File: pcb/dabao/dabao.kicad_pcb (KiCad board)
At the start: 2 copper layers, 127.4 x 114.6 mm, 76 parts, among them J1 Conn_01x05, J2 USB_C_Receptacle_USB2.0_16P, J3 Conn_01x04, J4 MagConn_01x04_Pin, J5 Conn_Battery, J7 Conn_01x04, J8 Display, SW1 SW_RESET, SW2 SW_POWER, U1 nice_nano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

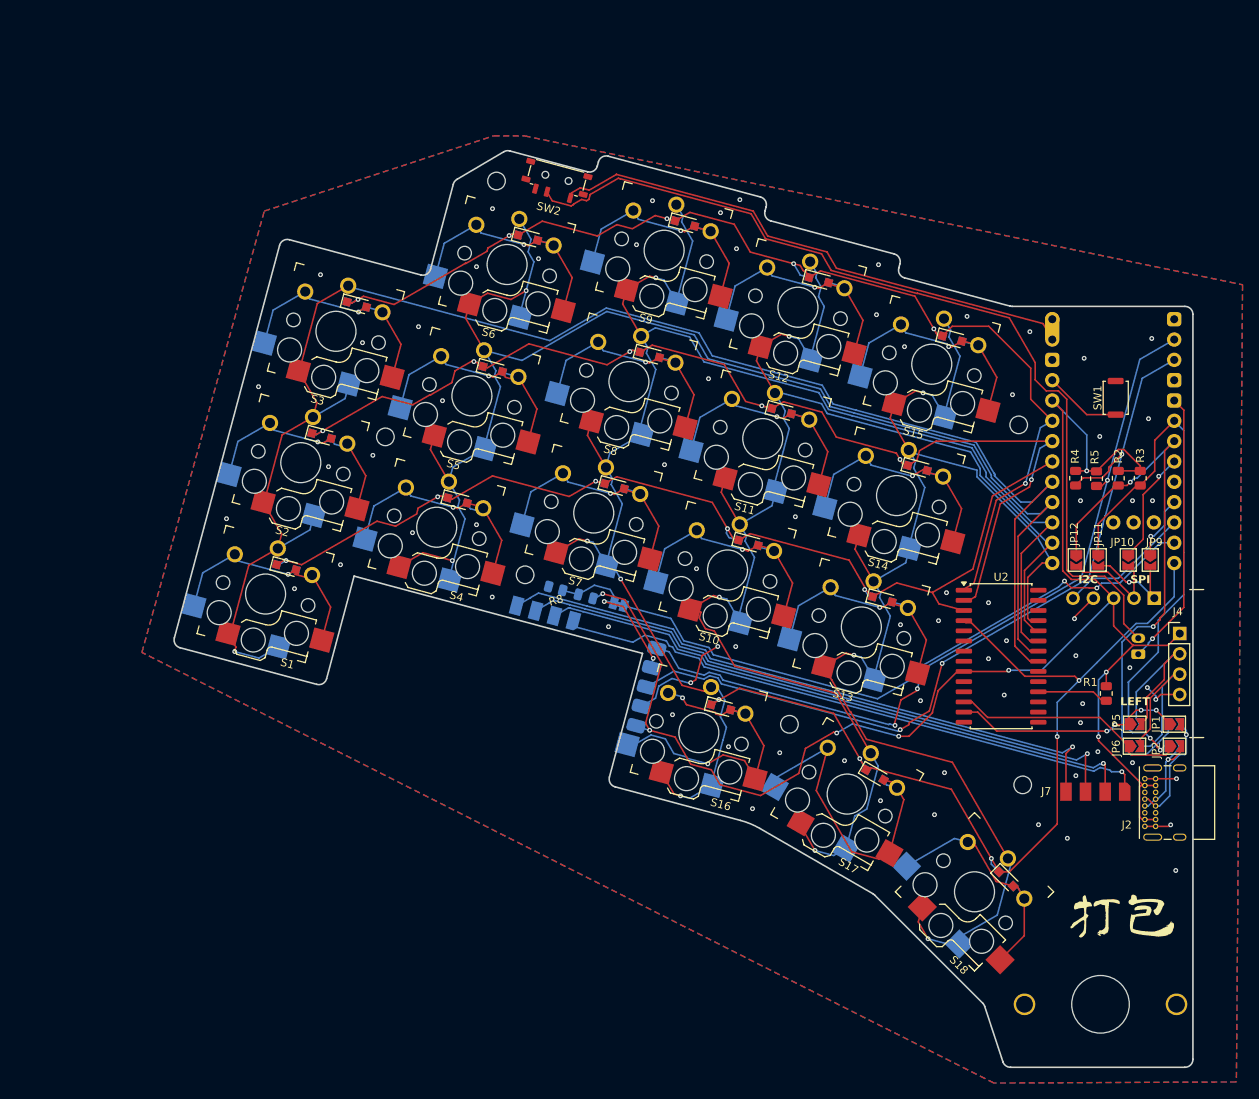
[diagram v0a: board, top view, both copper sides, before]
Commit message: Update outline for mounting holes
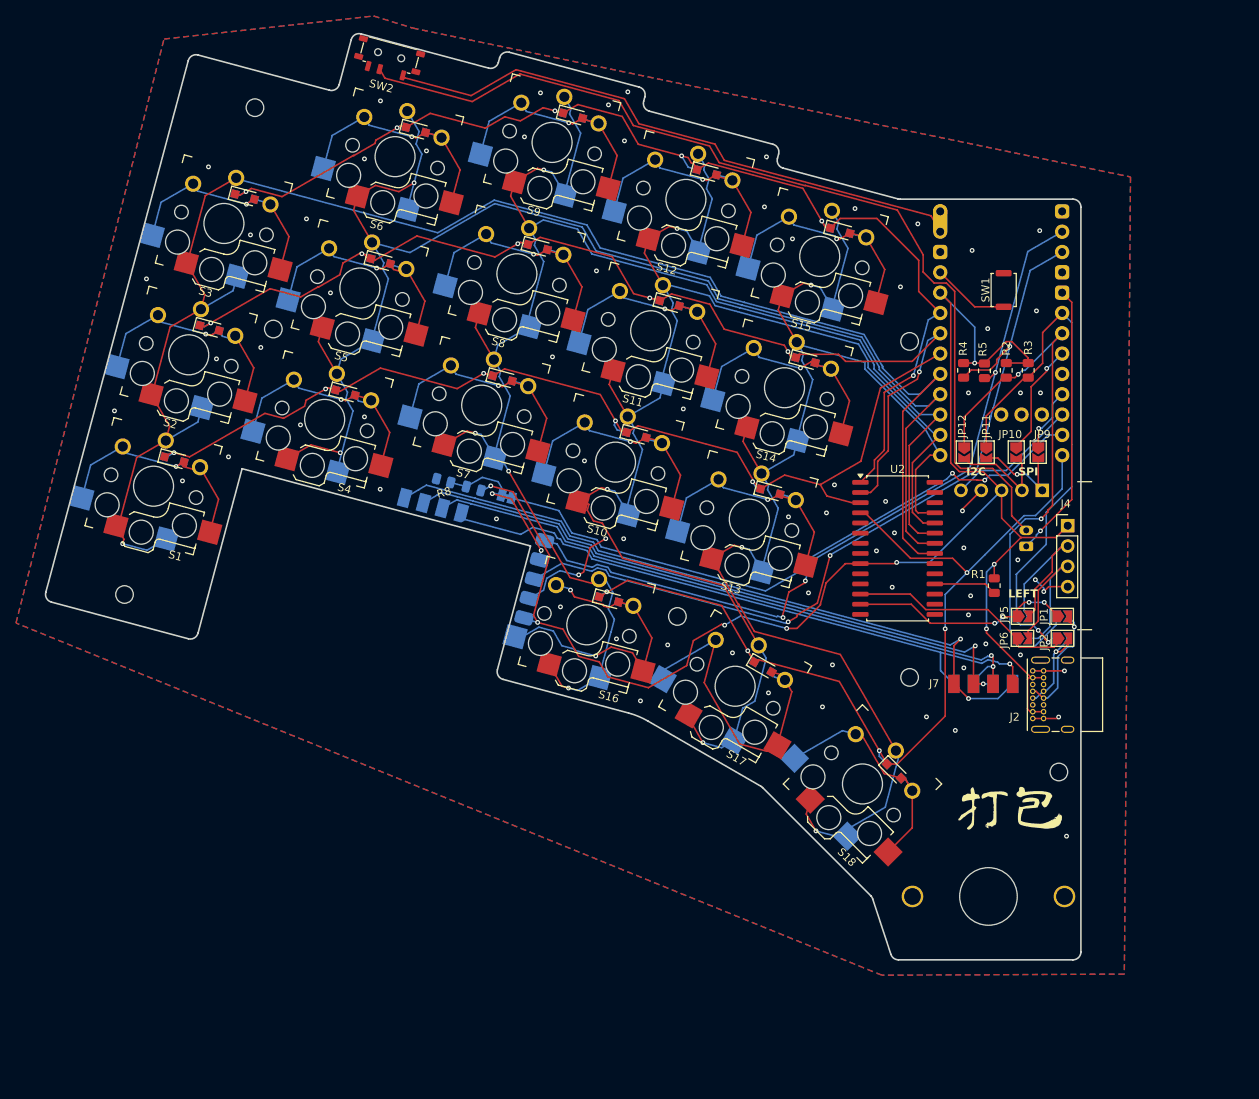
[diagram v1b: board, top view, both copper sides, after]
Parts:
- removed the REF** at (126.4, 98.2)
- added J6: Conn_01x04, Library:TPSensorModule_Connector, B.Cu at (183.7, 111.8)
- added REF**: MountingHole_2.2mm_M2, MountingHole:MountingHole_2.2mm_M2, F.Cu at (76.4, 100.7)
- added REF**: MountingHole_2.2mm_M2, MountingHole:MountingHole_2.2mm_M2, F.Cu at (193.2, 122.8)
- moved REF** 31.6 mm to (92.7, 39.8)
- moved SW2 25.9 mm to (109.5, 33.2)
- moved REF** 19.5 mm to (174.5, 111.0)
- moved S9 19.4 mm to (129.8, 44.1)
- moved D18 19.4 mm to (172.6, 122.7)
- moved D16 19.4 mm to (136.9, 101.3)
- moved G*** 19.4 mm to (186.8, 127.2)
- moved S14 19.4 mm to (158.9, 74.8)
- moved J7 19.4 mm to (183.7, 111.8)
- moved D1 19.4 mm to (82.6, 83.8)
- moved D7 19.4 mm to (123.6, 73.6)
- moved JP1 19.4 mm to (193.6, 103.4)
- moved JP10 19.4 mm to (187.8, 82.9)
- moved JP7 19.4 mm to (188.6, 103.4)
- moved D10 19.4 mm to (140.3, 80.7)
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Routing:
- net Net-(J3-Pin_4): track 80.0 -> 88.9 mm, vias 1 -> 2
- net /BAT+: track 67.4 -> 74.4 mm
- net Net-(J5-Pin_2): track 114.0 -> 120.7 mm
- net Net-(J3-Pin_1): track 75.7 -> 80.3 mm
- net Net-(J3-Pin_2): track 76.6 -> 80.2 mm, vias 1 -> 2
- net Net-(J3-Pin_3): track 78.6 -> 81.0 mm, vias 1 -> 2
- net /row_home: track 137.2 -> 138.9 mm
- net /SCL_Left: track 29.7 -> 28.6 mm
- net /SDA_Left: track 29.0 -> 27.9 mm
- net Net-(U2-~{RESET}): track 8.97 -> 7.90 mm
- net /row_thumb: track 119.0 -> 118.0 mm
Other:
- board size 127.4 x 114.6 mm -> 129.4 x 115.8 mm

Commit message: Revert "Update outline for mounting holes"
This reverts commit 8c40ebd10364a523e89f308933ebed6ba8cc3b75.
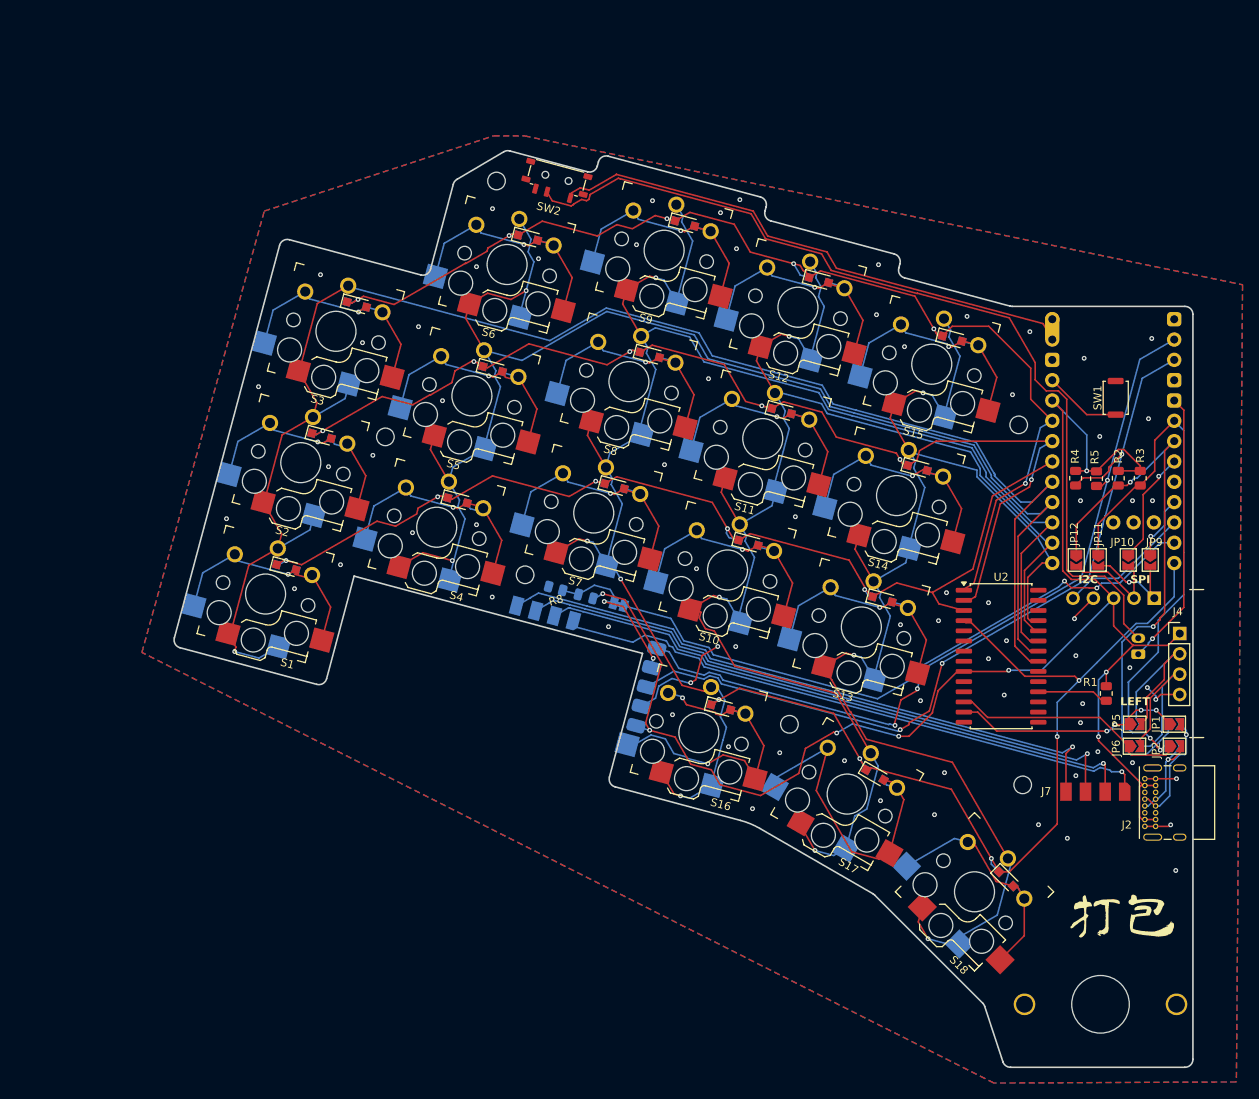
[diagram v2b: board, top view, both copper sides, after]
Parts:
- removed J6: Conn_01x04, Library:TPSensorModule_Connector
- removed the REF** at (76.4, 100.7)
- removed the REF** at (193.2, 122.8)
- added REF**: MountingHole_2.2mm_M2, MountingHole:MountingHole_2.2mm_M2, F.Cu at (126.4, 98.2)
- moved REF** 31.6 mm to (122.9, 49.0)
- moved SW2 25.9 mm to (130.4, 48.6)
- moved REF** 19.5 mm to (188.6, 124.5)
- moved S9 19.4 mm to (143.8, 57.6)
- moved D18 19.4 mm to (186.6, 136.2)
- moved D16 19.4 mm to (150.9, 114.8)
- moved G*** 19.4 mm to (200.8, 140.6)
- moved S14 19.4 mm to (172.9, 88.3)
- moved J7 19.4 mm to (197.7, 125.3)
- moved D1 19.4 mm to (96.6, 97.2)
- moved D7 19.4 mm to (137.6, 87.1)
- moved JP1 19.4 mm to (207.6, 116.9)
- moved JP10 19.4 mm to (201.8, 96.3)
- moved JP7 19.4 mm to (202.6, 116.9)
- moved D10 19.4 mm to (154.3, 94.2)
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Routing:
- net Net-(J3-Pin_4): track 88.9 -> 80.0 mm, vias 2 -> 1
- net /BAT+: track 74.4 -> 67.4 mm
- net Net-(J5-Pin_2): track 120.7 -> 114.0 mm
- net Net-(J3-Pin_1): track 80.3 -> 75.7 mm
- net Net-(J3-Pin_2): track 80.2 -> 76.6 mm, vias 2 -> 1
- net Net-(J3-Pin_3): track 81.0 -> 78.6 mm, vias 2 -> 1
- net /row_home: track 138.9 -> 137.2 mm
- net /SCL_Left: track 28.6 -> 29.7 mm
- net /SDA_Left: track 27.9 -> 29.0 mm
- net Net-(U2-~{RESET}): track 7.90 -> 8.97 mm
- net /row_thumb: track 118.0 -> 119.0 mm
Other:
- board size 129.4 x 115.8 mm -> 127.4 x 114.6 mm
